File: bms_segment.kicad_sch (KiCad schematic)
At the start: 101 parts, among them J1 Conn_02x17_Counter_Clockwise, J4 Conn_01x04, J5 Conn_01x04, J7 Conn_01x06, SW1 SW_Push, U1 LMR516xx, U2 MAX14921, U3 MAX11163, U4 REF61xx, U5 STM32F103C8Tx, U6 ADuM1252

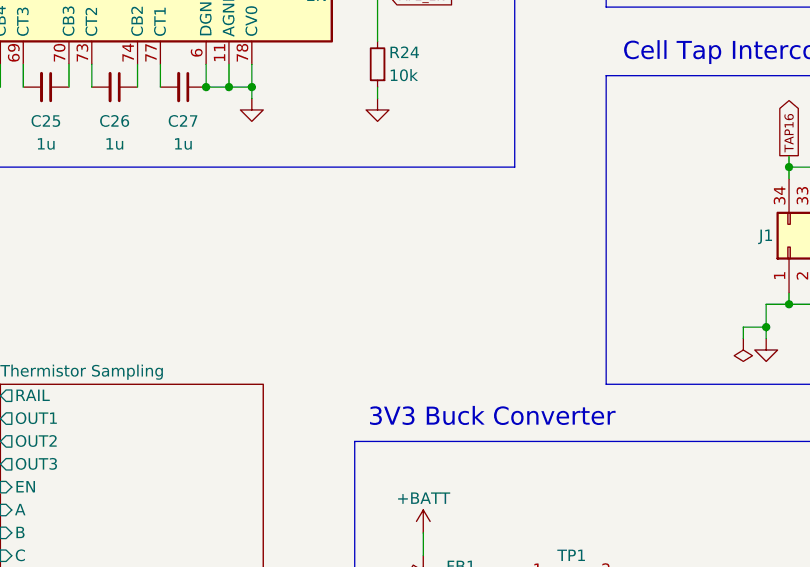
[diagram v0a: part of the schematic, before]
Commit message: Added keystone test point for GND
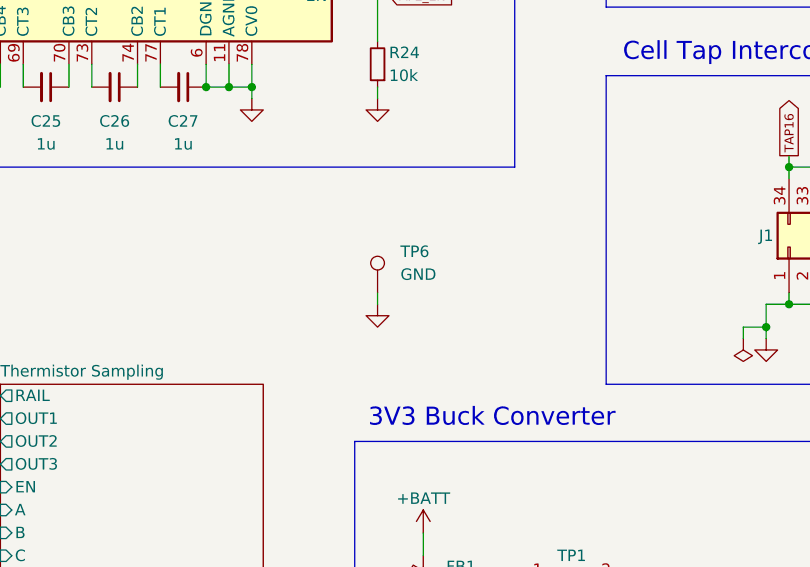
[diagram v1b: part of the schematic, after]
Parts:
- added TP6: GND, yfs:KEYSTONE_5019, symbol Connector:TestPoint
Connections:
- net GND: now also TP6.TP
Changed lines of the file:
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@@
 	(wire
 		(pts
+			(xy 179.07 101.6) (xy 179.07 102.87)
+		)
+		(stroke
+			(width 0)
+			(type default)
+		)
+	)
+	(wire
+		(pts
 			(xy 261.62 29.21) (xy 252.73 29.21)
 		)
@@
 	)
 	(symbol
+		(lib_id "Connector:TestPoint")
+		(at 179.07 101.6 0)
+		(unit 1)
+		(exclude_from_sim no)
+		(in_bom yes)
+		(on_board yes)
+		(dnp no)
+		(fields_autoplaced yes)
+		(property "Reference" "TP6"
+			(at 181.61 97.0279 0)
+			(effects
+				(font
+					(size 1.27 1.27)
+				)
+				(justify left)
+			)
+		)
+		(property "Value" "GND"
+			(at 181.61 99.5679 0)
+			(effects
+				(font
+					(size 1.27 1.27)
+				)
+				(justify left)
+			)
+		)
+		(property "Footprint" "yfs:KEYSTONE_5019"
+			(at 184.15 101.6 0)
+			(effects
+				(font
+					(size 1.27 1.27)
+				)
+				(hide yes)
+			)
+		)
+		(property "Datasheet" "~"
+			(at 184.15 101.6 0)
+			(effects
+				(font
+					(size 1.27 1.27)
+				)
+				(hide yes)
+			)
+		)
+		(property "Description" "test point"
+			(at 179.07 101.6 0)
+			(effects
+				(font
+					(size 1.27 1.27)
+				)
+				(hide yes)
+			)
+		)
+		(pin "TP"
+		)
+		(instances
+			(project "bms_segment"
+				(path "/ae4a7653-8e6d-4e05-b144-1e5e3b2092b7"
+					(reference "TP6")
+					(unit 1)
+				)
+			)
+		)
+	)
+	(symbol
 		(lib_id "Switch:SW_Push")
 		(at 154.94 182.88 0)
@@
 					(unit 1)
 				)
+			)
+		)
+	)
+	(symbol
+		(lib_id "power:GND")
+		(at 179.07 102.87 0)
+		(unit 1)
+		(exclude_from_sim no)
+		(in_bom yes)
+		(on_board yes)
+		(dnp no)
+		(fields_autoplaced yes)
+		(property "Reference" "#PWR06"
+			(at 179.07 109.22 0)
+			(effects
+				(font
+					(size 1.27 1.27)
+				)
+				(hide yes)
+			)
+		)
+		(property "Value" "GND"
+			(at 179.07 107.95 0)
+			(effects
+				(font
+					(size 1.27 1.27)
+				)
+				(hide yes)
+			)
+		)
+		(property "Footprint" ""
+			(at 179.07 102.87 0)
+			(effects
+				(font
+					(size 1.27 1.27)
+				)
+				(hide yes)
+			)
+		)
+		(property "Datasheet" ""
+			(at 179.07 102.87 0)
+			(effects
+				(font
+					(size 1.27 1.27)
+				)
+				(hide yes)
+			)
+		)
+		(property "Description" "Power symbol creates a global label with name \"GND\" , ground"
+			(at 179.07 102.87 0)
+			(effects
+				(font
+					(size 1.27 1.27)
+				)
+				(hide yes)
+			)
+		)
+		(pin "1"
+		)
+		(instances
+			(project "bms_segment"
+				(path "/ae4a7653-8e6d-4e05-b144-1e5e3b2092b7"
+					(reference "#PWR06")
+					(unit 1)
+				)

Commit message: *: Final cleanup for revision E
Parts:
- TP6: value GND -> TestPoint; footprint yfs:KEYSTONE_5019 -> TestPoint:TestPoint_Keystone_5019_Miniature
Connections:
- net GND: now also TP6.1; no longer TP6.TP
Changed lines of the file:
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@@
 		(on_board yes)
 		(dnp no)
-		(fields_autoplaced yes)
 		(property "Reference" "TP6"
-			(at 181.61 97.0279 0)
+			(at 177.165 95.885 0)
 			(effects
 				(font
@@
 			)
 		)
-		(property "Value" "GND"
+		(property "Value" "TestPoint"
 			(at 181.61 99.5679 0)
 			(effects
@@
 				)
 				(justify left)
+				(hide yes)
 			)
 		)
-		(property "Footprint" "yfs:KEYSTONE_5019"
+		(property "Footprint" "TestPoint:TestPoint_Keystone_5019_Miniature"
 			(at 184.15 101.6 0)
 			(effects
@@
 			)
 		)
-		(pin "TP"
+		(pin "1"
 		)
 		(instances

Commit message: *: Rework BOM
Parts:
- C1: DigiKey # (none) -> PCE3821CT-ND; Dist LCSC -> (none); Dist # C344075 -> (none); LCSC # (none) -> C344075; Mouser # (none) -> 667-EEE-FK1J220XP
- C10, C32, C35, C36, C37, C38, C39, C9: Dist LCSC -> (none); Dist # C5199872 -> (none); LCSC # (none) -> C5199872; Mouser # (none) -> 187-CL10B105KB8NQNC
- C11, C3: DigiKey # (none) -> 490-16315-1-ND; Dist LCSC -> (none); Dist # C405303 -> (none); LCSC # (none) -> C405303; Mouser # (none) -> 81-GRM31C5C2A104JA1L
- C12, C13, C14, C15, C16, C17, C18, C19, C20, C21, C22, C23, C24, C25, C26, C27: DigiKey # (none) -> 490-10675-1-ND; Dist LCSC -> (none); Dist # C126592 -> (none); LCSC # (none) -> C126592; Mouser # (none) -> 81-GCM21BR71H105KA3L
- C2: DigiKey # (none) -> 490-3385-1-ND; Dist LCSC -> (none); Dist # C86054 -> (none); LCSC # (none) -> C86054; Mouser # (none) -> 81-GRM32ER72A225KA35
- C28: DigiKey # (none) -> 490-4771-1-ND; Dist LCSC -> (none); Dist # C126576 -> (none); LCSC # (none) -> C126576; Mouser # (none) -> 81-GCM1885C2A101JA6D
- C29, C30, C31, C4, C40, C41, C42: DigiKey # (none) -> 1276-1000-1-ND; Dist LCSC -> (none); Dist # C1591 -> (none); LCSC # (none) -> C1591; Mouser # (none) -> 187-CL10B104KB8NNNC
- C33, C34: Dist LCSC -> (none); Dist # C97954 -> (none); LCSC # (none) -> C97954
- C6, C7, C8: DigiKey # (none) -> 490-5313-1-ND; Dist LCSC -> (none); Dist # C21397 -> (none); LCSC # (none) -> C21397; Mouser # (none) -> 81-GRM32ER71E226KE5L
- D17: Dist LCSC -> (none); Dist # C84263 -> (none); LCSC # (none) -> C84263
- F1: DigiKey # (none) -> F8130CT-ND; Dist LCSC -> (none); Dist # C2153714 -> (none); LCSC # (none) -> C2153714; Mouser # (none) -> 576-1206L010/60WR
- FB1: DigiKey # (none) -> 490-5258-1-ND; Dist LCSC -> (none); Dist # C85833 -> (none); LCSC # (none) -> C85833; Mouser # (none) -> 81-BLM18KG601SN1D
- FB2: DigiKey # (none) -> 490-5221-1-ND; Dist LCSC -> (none); Dist # C80165 -> (none); LCSC # (none) -> C80165; Mouser # (none) -> 81-BLM18PG221SN1D
- J4, J5: DigiKey # (none) -> 900-2125280400-ND; Dist LCSC -> (none); Dist # C131334 -> (none); Mfr JST -> Molex; Mfr # B4B-PH-K-S(LF)(SN) -> 2125280400; Mouser # (none) -> 538-212528-0400
- J6: renamed from J7; Dist LCSC -> (none); Dist # C42372545 -> (none); LCSC # (none) -> C42372545
- L1: DigiKey # (none) -> 541-2579-1-ND; Dist Mouser -> (none); Dist # 70-IHLP2525CZR220M1A -> (none); Mouser # (none) -> 70-IHLP2525CZR220M1A
- R23, R24, R26, R75, R76, R78, R79: Dist LCSC -> (none); Dist # C25804 -> (none); LCSC # (none) -> C25804
- R77: Dist LCSC -> (none); Dist # C23138 -> (none); LCSC # (none) -> C23138
- RN13, RN14, RN15, RN16, RN17, RN18, RN19, RN20: DigiKey # (none) -> EXB-V8V302JV-ND; LCSC # (none) -> C1732445; Mfr (none) -> Panasonic; Mfr # (none) -> EXB-V8V302JV; Mouser # (none) -> 667-EXB-V8V302JV
- SW1: DigiKey # (none) -> 4809-SKRPACE010CT-ND; Dist LCSC -> (none); Dist # C139797 -> (none); LCSC # (none) -> C139797; Mouser # (none) -> 688-SKRPACE010
- TP6: DigiKey # (none) -> 36-5019CT-ND; LCSC # (none) -> C238131; Mfr (none) -> Keystone Electronics; Mfr # (none) -> 5019; Mouser # (none) -> 534-5019
- U1: DigiKey # (none) -> 296-LMR51606XDBVRCT-ND; Dist Mouser -> (none); Dist # 595-LMR51606XDBVR -> (none); LCSC # (none) -> C21260865; Mouser # (none) -> 595-LMR51606XDBVR
- U2: DigiKey # (none) -> 175-MAX14921ECS+TCT-ND; LCSC # (none) -> C2932577; Mfr (none) -> Analog Devices; Mfr # (none) -> MAX14921ECS+T; Mouser # (none) -> 700-MAX14921ECS+T
- U3: DigiKey # (none) -> 175-MAX11163EUB+TCT-ND; Dist Mouser -> (none); Dist # 700-MAX11163EUB+ -> (none); LCSC # (none) -> C2670420; Mfr # MAX11163EUB+ -> MAX11163EUB+T; Mouser # (none) -> 700-MAX11163EUB+T
- U4: DigiKey # (none) -> 296-51531-1-ND; Dist Mouser -> (none); Dist # 595-REF6145IDGKT -> (none); LCSC # (none) -> C2157054; Mfr # REF6145IDGKT -> REF6045IDGKR; Mouser # (none) -> 595-REF6045IDGKR
- U5: DigiKey # (none) -> 497-17666-1-ND; Dist LCSC -> (none); Dist # C8734 -> (none); LCSC # (none) -> C8734; Mouser # (none) -> 511-STM32F103C8T6
- U6: DigiKey # (none) -> 505-ADUM1252AUA+TCT-ND; Dist Mouser -> (none); Dist # 584-ADUM1252AUA+ -> (none); Mfr # ADUM1252AUA+ -> ADUM1252AUA+T; Mouser # (none) -> 584-ADUM1252AUA+T

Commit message: schematic: Cleanup BOM
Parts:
- C5, R6, TP1, TP2, TP3, TP4, TP5: now left out of the parts list
- J1: Mfr (none) -> Samtec; Mfr # (none) -> TW-17-03-F-D-275-090
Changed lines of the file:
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@@
 		(unit 1)
 		(exclude_from_sim no)
-		(in_bom yes)
+		(in_bom no)
 		(on_board yes)
 		(dnp no)
@@
 		(unit 1)
 		(exclude_from_sim no)
-		(in_bom yes)
+		(in_bom no)
 		(on_board yes)
 		(dnp no)
@@
 		(unit 1)
 		(exclude_from_sim no)
-		(in_bom yes)
+		(in_bom no)
 		(on_board yes)
 		(dnp no)
@@
 		(unit 1)
 		(exclude_from_sim no)
-		(in_bom yes)
+		(in_bom no)
 		(on_board yes)
 		(dnp no)
@@
 		(unit 1)
 		(exclude_from_sim no)
-		(in_bom yes)
+		(in_bom no)
 		(on_board yes)
 		(dnp no)
@@
 		(unit 1)
 		(exclude_from_sim no)
-		(in_bom yes)
+		(in_bom no)
 		(on_board yes)
 		(dnp no)
@@
 			)
 		)
+		(property "Mfr" "Samtec"
+			(at 245.11 96.52 90)
+			(effects
+				(font
+					(size 1.27 1.27)
+				)
+				(hide yes)
+			)
+		)
+		(property "Mfr #" "TW-17-03-F-D-275-090"
+			(at 245.11 96.52 90)
+			(effects
+				(font
+					(size 1.27 1.27)
+				)
+				(hide yes)
+			)
+		)
 		(pin "1"
 		)
@@
 		(unit 1)
 		(exclude_from_sim no)
-		(in_bom yes)
+		(in_bom no)
 		(on_board yes)
 		(dnp no)
